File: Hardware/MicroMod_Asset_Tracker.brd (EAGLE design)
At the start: 76.2 x 76.2 mm, 336 parts, among them J11 microSD, J13 TP, J17 NANO_SIM, J18 SARA_USB, J19 NI, J2 JTAG, J4 MICROMOD-2222-C, J5 SPI, J6 DIAG, J7 QWIIC_RIGHT_ANGLE, J9 !RST!, Q1 310mA/60V/1.6Ω, Q10 20V/0.2A/8MHz/1.2Ω/1Vth, Q2 310mA/60V/1.6Ω, Q3 310mA/60V/1.6Ω, Q4 310mA/60V/1.6Ω, Q5 20V/0.2A/8MHz/1.2Ω/1Vth, Q6 20V/4.2A/52mΩ/1.4W, Q7 310mA/60V/1.6Ω, U1 SARA-R5, U13 9DoF IMU, U14 1.8V/100mA, U2 MCP73831, U3 3.3V, U4 TXB0104, U5 AP7361C-33FGE, U6 TXB0104, U7 PCA9306, U8 74HC1G04, U9 TXB0104

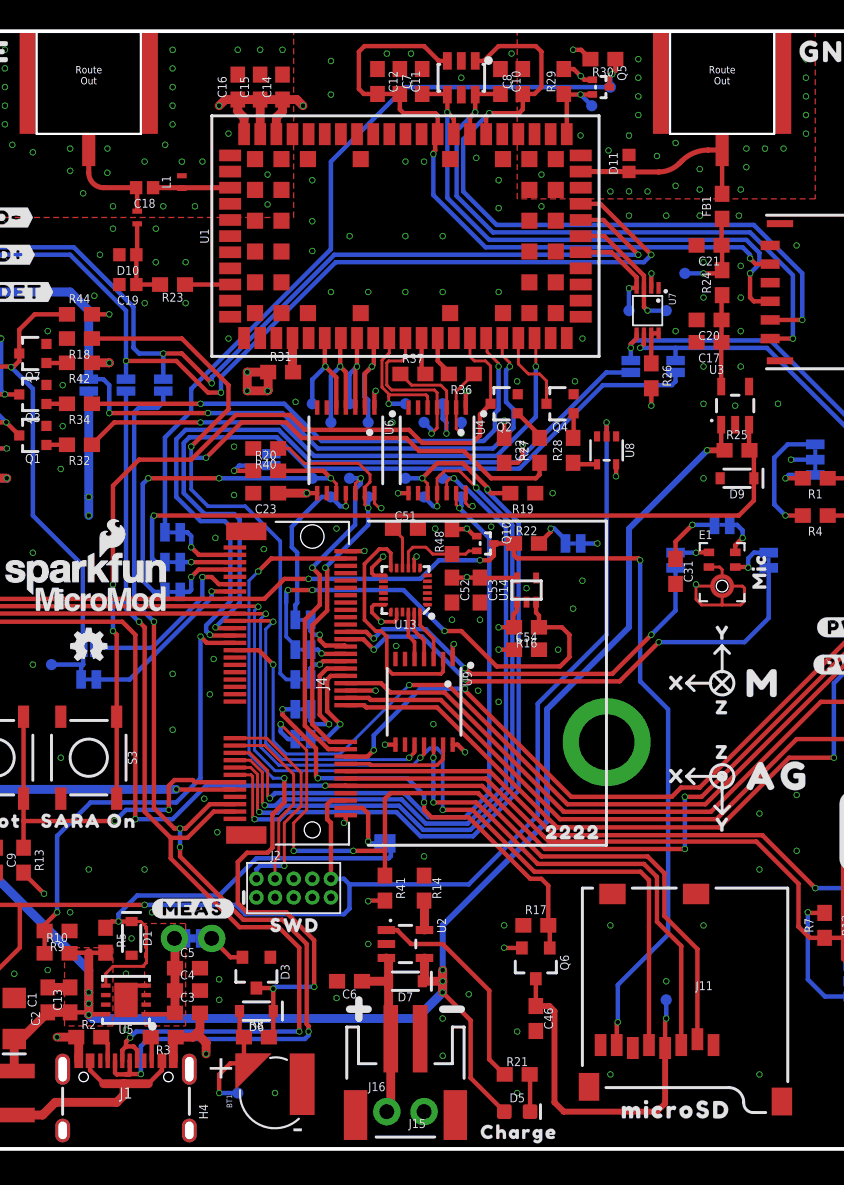
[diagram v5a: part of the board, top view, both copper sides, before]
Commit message: Replaced the Level Shifters
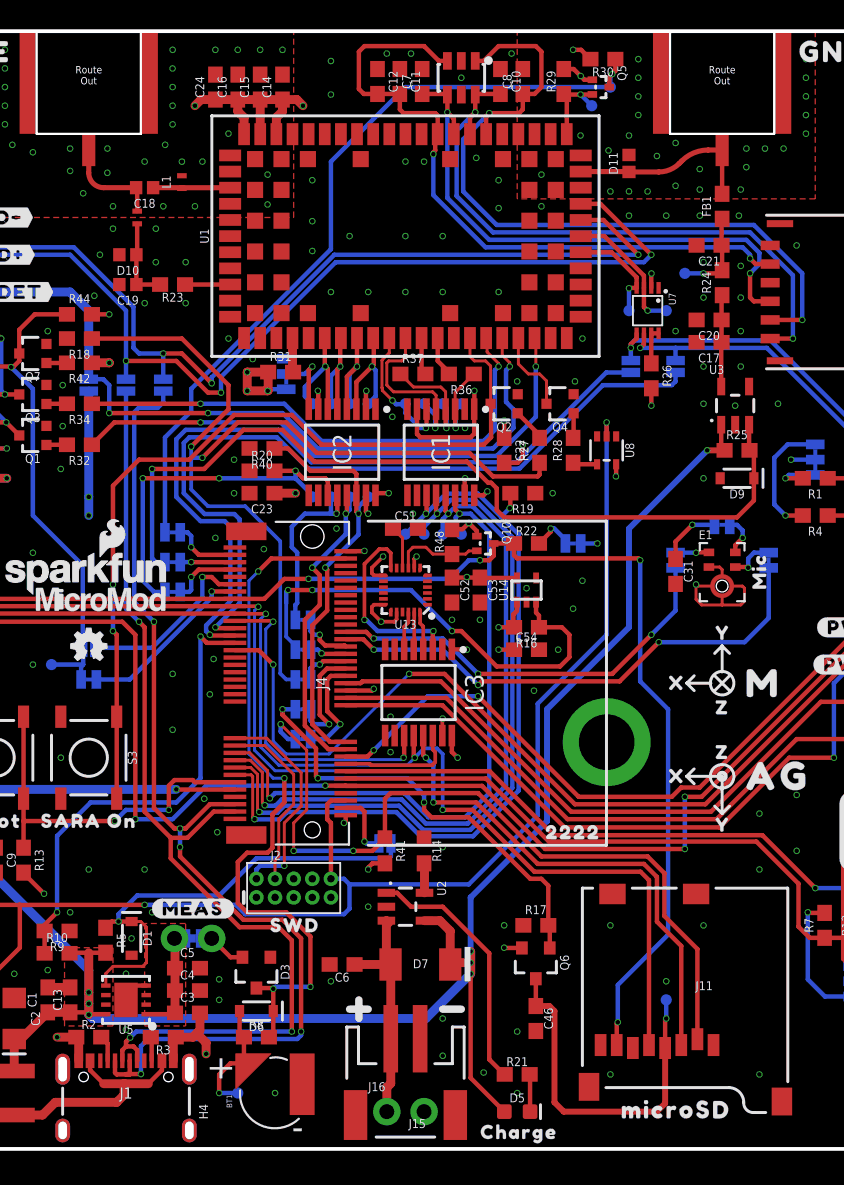
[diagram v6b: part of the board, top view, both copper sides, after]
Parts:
- removed JP9: JUMPER-SMT_2_NO_SILK, SparkFun-Jumpers:SMT-JUMPER_2_NO_SILK
- removed U4, U6, U9: TXB0104, SparkFun-IC-Comms:TSSOP14
- added C24: 15pF, SparkFun-Capacitors:0603
- added IC1, IC2, IC3: SN74AVC4T774PW, New_Parts:SOP65P640X120-16N
- added JP22: JUMPER-SMT_3_1-NC_TRACE_SILK, SparkFun-Jumpers:SMT-JUMPER_3_1-NC_TRACE_SILK
- C15: value 47pF -> 68pF
- C3: value 1.0uF -> 4.7uF
- D7: value 3A/10V/280mV -> 1A/15V/220mV; device SparkFun-DiscreteSemi:SOD-323 -> SparkFun-DiscreteSemi:DO-214BA
- moved U$102 8.94 mm to (27.2, 53.0), turned to 0 degrees
- moved TP6 3.81 mm to (40.6, 41.9)
- moved TP8 3.81 mm to (38.1, 41.9)
- moved TP5 2.54 mm to (41.9, 41.9)
- moved TP7 2.54 mm to (39.4, 41.9)
- moved U2 2.54 mm to (38.1, 16.5)
- moved R14 2.54 mm to (39.4, 20.3)
- moved R41 2.54 mm to (36.7, 20.3)
- moved D7 1.53 mm to (39.1, 12.6), turned to 0 degrees
- moved TP1 1.27 mm to (41.9, 50.8)
- moved TP14 1.27 mm to (35.6, 50.8)
- moved TP16 1.27 mm to (33.0, 50.8)
- moved TP19 1.27 mm to (34.3, 44.5)
- moved TP21 1.27 mm to (31.8, 44.5)
- moved TP3 1.27 mm to (39.4, 50.8)
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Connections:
- removed net N$18: JP9.2, R20.1
- new net N$23: IC2.8, JP22.2
- net 1.8V: now also IC3.1, IC3.16; no longer U9.1, U9.8
- net 3.3V: now also C24.1, IC1.15, IC2.15, IC3.15; no longer U4.14, U6.14, U9.14
- net CTS1: now also IC1.12; no longer U4.11
- net DCD: now also IC2.13; no longer U6.12
- net DSR: now also IC2.11; no longer U6.10
- net DTR: now also IC2.14; no longer U6.13
- net GND: now also C24.2, IC1.10, IC1.2, IC1.8, IC1.9, IC2.1, IC2.10, IC2.9, IC3.10, IC3.2, IC3.7, IC3.8, IC3.9, JP22.1, R20.1; no longer JP9.1, U4.7, U6.7, U9.7
- net ICM-20948-LV_!CS!: now also IC3.6; no longer U9.5
- net ICM-20948-LV_INT: now also IC3.3; no longer U9.2
- net ICM-20948-LV_SCK: now also IC3.5; no longer U9.4
- net ICM-20948-LV_SDI: now also IC3.4; no longer U9.3
- net ICM_!CS!: now also IC3.11; no longer U9.10
- net ICM_INT: now also IC3.14; no longer U9.13
- net RI: now also IC2.12; no longer U6.11
- net RTS1: now also IC1.11; no longer U4.10
- net RX1: now also IC1.14; no longer U4.13
- net SARA_CTS: now also IC1.5; no longer U4.4
- net SARA_DCD/RXD2O: now also IC2.4; no longer U6.3
- net SARA_DSR/RTS2I: now also IC2.6; no longer U6.5
- net SARA_DTR/TXD2I: now also IC2.3; no longer U6.2
- net SARA_RI/CTS2O: now also IC2.5; no longer U6.4
- net SARA_RTS: now also IC1.6; no longer U4.5
- net SARA_RXD: now also IC1.3; no longer U4.2
- net SARA_TXD: now also IC1.4; no longer U4.3
- net SPI_SCK: now also IC3.12; no longer U9.11
- net SPI_SDO: now also IC3.13; no longer U9.12
- net TX1: now also IC1.13; no longer U4.12
- net VCCIO: now also IC1.1, IC1.16, IC1.7, IC2.16, IC2.2, IC2.7, JP22.3; no longer U4.1, U4.8, U6.1, U6.8
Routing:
- net VCCIO: track 144.9 -> 161.3 mm, vias 12 -> 14
- net ANT_GNSS_PWR_EN: track 50.6 -> 58.3 mm
- net N$23: track 0.00 -> 4.99 mm, vias 0 -> 1
- net N$18: track 4.00 -> 0.00 mm, vias 1 -> 0
- net V_BATT: track 12.5 -> 16.1 mm
- net VIN: track 172.9 -> 176.5 mm
- net ICM-20948-LV_INT: track 16.2 -> 13.4 mm, vias 0 -> 2
- net CHG_LED: track 14.9 -> 17.4 mm
- net DCD: track 24.2 -> 22.0 mm
- net SD_!CS!: track 56.7 -> 54.5 mm
- net 3.3V: track 67.2 -> 69.2 mm
- net 1.8V: track 98.0 -> 100.0 mm
- net SARA_RI/CTS2O: track 8.99 -> 7.75 mm
- net CTS1: track 51.6 -> 50.4 mm, vias 3 -> 2
- net RX1: track 43.4 -> 44.5 mm
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
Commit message: Ready for review
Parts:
- added U$132: MAX17048, SparkFun-IC-Power:DFN-8
- moved C6 1.40 mm to (33.7, 11.2)
- renumbered JP22 to DSR
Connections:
- net GND: now also U$132.P$1, U$132.P$4, U$132.P$6, U$132.P$9
- net I2C_SCL: now also U$132.P$7
- net I2C_SDA: now also U$132.P$8
- net V_BATT: now also U$132.P$2, U$132.P$3
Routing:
- net I2C_SDA: track 57.7 -> 76.2 mm, vias 0 -> 2
- net I2C_SCL: track 54.3 -> 72.7 mm, vias 1 -> 3
- net V_BATT: track 16.1 -> 19.7 mm
- net !RESET!: track 113.9 -> 112.5 mm
- net USB_D-: track 73.4 -> 72.8 mm
- net USB_D+: track 69.6 -> 69.1 mm
- net RTC_3V: track 49.3 -> 48.7 mm
- net GND: vias 190 -> 191
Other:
- board text added: "Dimensions are in inches"
